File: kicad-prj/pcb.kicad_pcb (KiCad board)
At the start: 2 copper layers, 131.6 x 93.2 mm, 48 parts

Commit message: dev: remove diode silkscreens
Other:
- net class Default removed

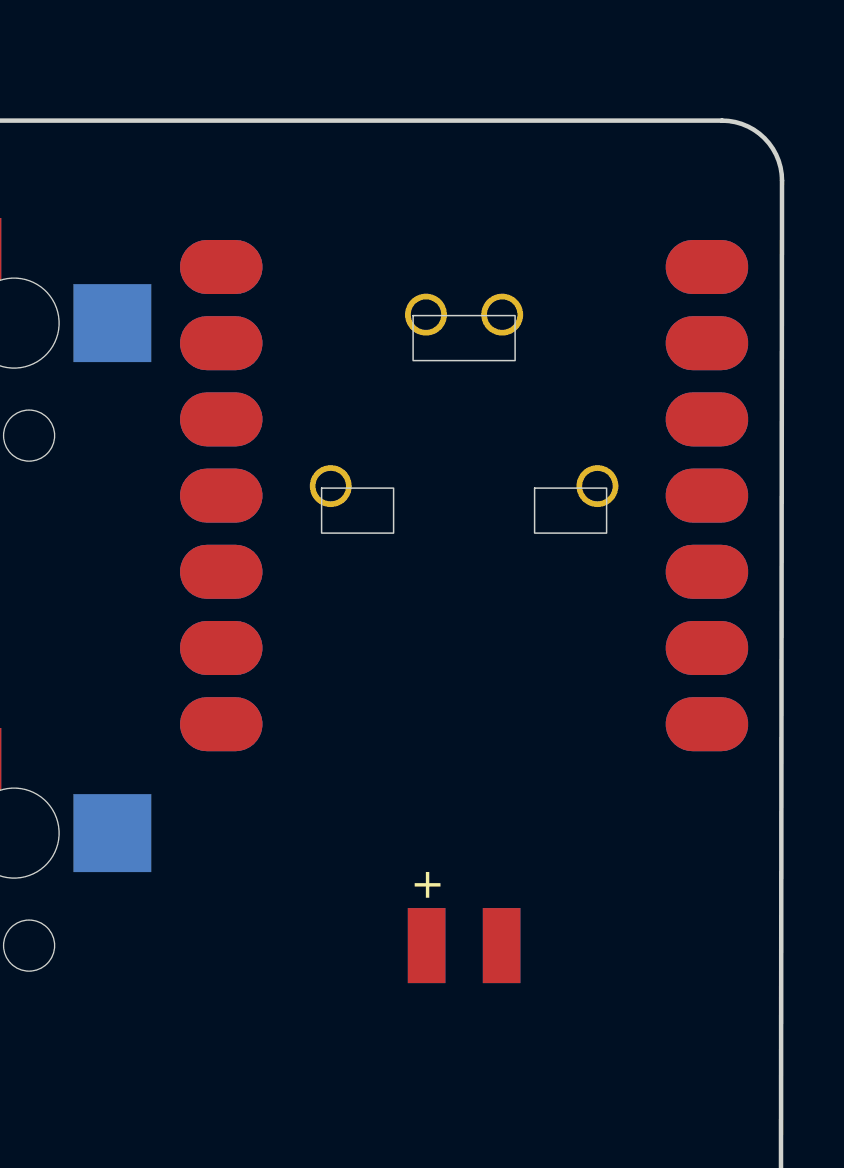
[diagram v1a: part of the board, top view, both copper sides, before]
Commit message: dev: wired up mcu pads on pcb
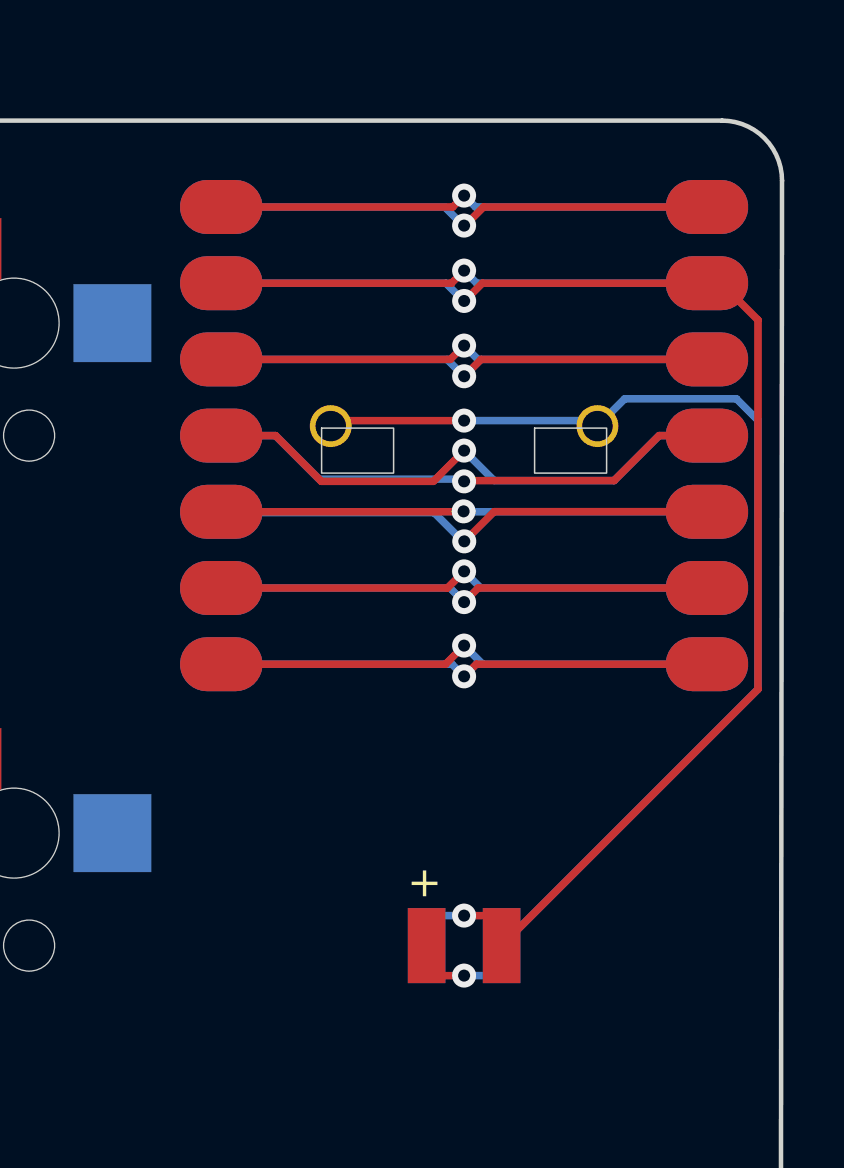
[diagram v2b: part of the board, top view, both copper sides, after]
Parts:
- moved MCU1 2.00 mm to (280.0, 121.0)
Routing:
- net GND: track 0.00 -> 47.1 mm, vias 0 -> 2
- net BAT+: track 0.00 -> 38.6 mm, vias 0 -> 2
- net rthumbs: track 0.00 -> 19.2 mm, vias 0 -> 1
- net 5V: track 0.00 -> 18.5 mm, vias 0 -> 1
- net cpinky: track 0.00 -> 18.4 mm, vias 0 -> 1
- net 3V3: track 0.00 -> 18.4 mm, vias 0 -> 1
- net cring: track 0.00 -> 18.0 mm, vias 0 -> 1
- net cinner: track 0.00 -> 17.7 mm, vias 0 -> 1
- net scl: track 0.00 -> 17.6 mm, vias 0 -> 1
- net cmiddle: track 0.00 -> 17.5 mm, vias 0 -> 1
- net rbottom: track 0.00 -> 17.5 mm, vias 0 -> 1
- net rhome: track 0.00 -> 17.5 mm, vias 0 -> 1
- net cindex: track 0.00 -> 17.5 mm, vias 0 -> 1
- net rtop: track 0.00 -> 17.5 mm, vias 0 -> 1
- net sda: track 0.00 -> 17.2 mm, vias 0 -> 1

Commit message: dev: wire up key matrix
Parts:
- moved Di12 2.97 mm to (239.4, 158.5)
- moved Di3 2.97 mm to (185.4, 168.5)
- moved S10 2.97 mm to (221.4, 129.5)
- moved S12 2.97 mm to (239.4, 153.5)
- moved Di20 2.97 mm to (271.2, 185.8)
- moved Di15 2.97 mm to (257.4, 158.5)
- moved MCU1 2.97 mm to (277.4, 119.5)
- moved S16 2.97 mm to (257.4, 136.5)
- moved Di18 2.97 mm to (233.4, 175.5)
- moved Di9 2.97 mm to (221.4, 151.5)
- moved S4 2.97 mm to (185.4, 146.5)
- moved S17 2.97 mm to (257.4, 119.5)
- moved Di10 2.97 mm to (221.4, 134.5)
- moved Di11 2.97 mm to (221.4, 117.5)
- moved Di14 2.97 mm to (239.4, 124.5)
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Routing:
- net rthumbs: track 19.2 -> 250.2 mm
- net cring: track 18.0 -> 208.1 mm, vias 1 -> 7
- net cpinky: track 18.4 -> 202.4 mm, vias 1 -> 5
- net cmiddle: track 17.5 -> 161.1 mm, vias 1 -> 6
- net rbottom: track 17.5 -> 149.4 mm
- net cindex: track 17.5 -> 140.0 mm, vias 1 -> 6
- net rhome: track 17.5 -> 133.5 mm
- net cinner: track 17.7 -> 131.3 mm, vias 1 -> 7
- net rtop: track 17.5 -> 118.6 mm
- net index_bottom: track 0.00 -> 25.8 mm, vias 0 -> 1
- net inner_bottom: track 0.00 -> 25.8 mm, vias 0 -> 2
- net pinky_top: track 0.00 -> 25.8 mm, vias 0 -> 1
- net inner_top: track 0.00 -> 25.7 mm, vias 0 -> 1
- net ring_bottom: track 0.00 -> 25.7 mm, vias 0 -> 1
- net left_cluster: track 0.00 -> 25.6 mm
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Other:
- board size 131.6 x 93.2 mm -> 131.6 x 93.3 mm

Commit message: dev: include reversible oled screen
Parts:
- added REF**: PinHeader_1x04_P2.54mm_Vertical, Connector_PinHeader_2.54mm:PinHeader_1x04_P2.54mm_Vertical, F.Cu at (273.5, 148.5)
- added REF**: SolderJumper-2_P1.3mm_Open_TrianglePad1.0x1.5mm, Jumper:SolderJumper-2_P1.3mm_Open_TrianglePad1.0x1.5mm, F.Cu at (273.5, 145.5)
- added REF**: SolderJumper-2_P1.3mm_Open_TrianglePad1.0x1.5mm, Jumper:SolderJumper-2_P1.3mm_Open_TrianglePad1.0x1.5mm, F.Cu at (278.5, 145.5)
- added REF**: SolderJumper-2_P1.3mm_Open_TrianglePad1.0x1.5mm, Jumper:SolderJumper-2_P1.3mm_Open_TrianglePad1.0x1.5mm, F.Cu at (276.0, 145.5)
- added REF**: SolderJumper-2_P1.3mm_Open_TrianglePad1.0x1.5mm, Jumper:SolderJumper-2_P1.3mm_Open_TrianglePad1.0x1.5mm, F.Cu at (281.0, 145.5)
- added REF**: SolderJumper-2_P1.3mm_Open_TrianglePad1.0x1.5mm, Jumper:SolderJumper-2_P1.3mm_Open_TrianglePad1.0x1.5mm, B.Cu at (281.0, 145.5)
- added REF**: SolderJumper-2_P1.3mm_Open_TrianglePad1.0x1.5mm, Jumper:SolderJumper-2_P1.3mm_Open_TrianglePad1.0x1.5mm, B.Cu at (278.5, 145.5)
- added REF**: SolderJumper-2_P1.3mm_Open_TrianglePad1.0x1.5mm, Jumper:SolderJumper-2_P1.3mm_Open_TrianglePad1.0x1.5mm, B.Cu at (276.0, 145.5)
- added REF**: SolderJumper-2_P1.3mm_Open_TrianglePad1.0x1.5mm, Jumper:SolderJumper-2_P1.3mm_Open_TrianglePad1.0x1.5mm, B.Cu at (273.5, 145.5)
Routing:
- net sda: track 17.2 -> 71.3 mm
- net 5V: track 18.5 -> 62.8 mm, vias 1 -> 2
- net scl: track 17.6 -> 47.9 mm, vias 1 -> 2
- net GND: track 47.1 -> 68.1 mm, vias 2 -> 3
- net oled4: track 0.00 -> 4.65 mm
- net oled3: track 0.00 -> 4.62 mm
- net oled2: track 0.00 -> 4.58 mm
- net oled1: track 0.00 -> 4.55 mm
- net BAT+: track 38.6 -> 42.8 mm, vias 2 -> 4

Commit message: dev: add kicad outputs
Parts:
- added G***: LOGO, my-graphics:porsche-front-big, F.Cu at (215.0, 136.5)
- added G***: LOGO, my-graphics:porsche-back-big, B.Cu at (212.5, 137.0)
- REF**: value PinHeader_1x04_P2.54mm_Vertical -> PinHeader_1x04_P2.54mm_Vertical_custom
